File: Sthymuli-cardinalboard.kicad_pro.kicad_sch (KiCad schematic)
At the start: 38 parts, among them J8 Conn_02x08_Counter_Clockwise, Q10 NX7002AK, Q11 NX7002AK, Q12 NX7002AK, Q13 NX7002AK, SW10 SW_Push, SW7 SW_Push, SW8 SW_Push, SW9 SW_Push, U13 LSM6DS3, U17 ITR9909, U18 ITR9909, U19 ITR9909, U20 ITR9909

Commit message: routing small board
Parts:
- removed Q12, Q13: NX7002AK, Package_TO_SOT_SMD:SOT-23, symbol Transistor_FET_Other:Q_NMOS_Depletion_GSD
- removed R54, R55: 3K3, Capacitor_SMD:C_0201_0603Metric, symbol Device:R
- removed R64, R65: 27R, Capacitor_SMD:C_0201_0603Metric, symbol Device:R
- removed SW10, SW9: SW_Push, sthymuli:XKB5858, symbol Switch:SW_Push
- removed U19, U20: ITR9909, sthymuli:ITR_9909_Vertical, symbol kitprisme:ITR9909
- J1: renamed from J8; footprint (none) -> Connector_PinSocket_2.54mm:PinSocket_2x08_P2.54mm_Vertical_SMD
- U2: renamed from U18; footprint sthymuli:ITR_9909_Horizontal -> sthymuli:ITR_9909_Vertical
- renumbered C20 to C1, C21 to C2, C22 to C3, C23 to C4, C24 to C5, C25 to C6, C77 to C7, D20 to D1, D26 to D2, D21 to D3, D22 to D4, D23 to D5, D24 to D6, D25 to D7, Q10 to Q1, Q11 to Q2, R52 to R1, R53 to R2, R62 to R3, R63 to R4, SW7 to SW1, SW8 to SW2, U17 to U1, U13 to U3
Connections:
- net ACC_B_INT1 is gone; now on net +3V3: J1.2 (Pin_2)
- net btn_EAST_DOWN is gone; now on net btn_DOWN: J1.4 (Pin_4)
- net btn_EAST_UP is gone; now on net IR_TRA_VERT: J1.13 (Pin_13)
- net +3V3: no longer J1.1 (Pin_1)
- net +5V: now also J1.1 (Pin_1); no longer J1.16 (Pin_16)
- net BAT+: now also J1.6 (Pin_6); no longer J1.7 (Pin_7)
- net BAT-: now also J1.7 (Pin_7); no longer J1.10 (Pin_10)
- net DIN: now also J1.8 (Pin_8); no longer J1.3 (Pin_3)
- net DOUT: now also J1.9 (Pin_9); no longer J1.14 (Pin_14)
- net GND: now also J1.3 (Pin_3); no longer J1.15 (Pin_15)
- net SCL: now also J1.15 (Pin_15); no longer J1.9 (Pin_9)
- net SDA: now also J1.14 (Pin_14); no longer J1.8 (Pin_8)
- net btn_UP: now also J1.5 (Pin_5)
- net ACC_INT: now reaches U3.4 (INT1)
- net ACC_INT: now also J1.16 (Pin_16)
- net IR_REC_2 renamed IR_REC_HORI
- net IR_REC_HORI: now also J1.10 (Pin_10); no longer J1.5 (Pin_5)
- net IR_REC_3 renamed IR_REC_VERT
- net IR_REC_VERT: now also J1.12 (Pin_12); no longer J1.6 (Pin_6)
- net IR_TRA_2 renamed IR_TRA_HORI
- net IR_TRA_HORI: now also J1.11 (Pin_11); no longer J1.12 (Pin_12)
- net IR_TRA_3 renamed IR_TRA_VERT
- net IR_TRA_VERT: no longer J1.11 (Pin_11)
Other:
- note removed: "Buttons/switch"
- note removed: "we use MCP23017 internal pull-ups"
- moved on the sheet: BT1, C1, C2, C3, C4, C5, C6, C7, D1, D2, D3, D4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

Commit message: tried autoroute...
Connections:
- net btn_DOWN renamed btn_A
- net btn_UP renamed btn_B
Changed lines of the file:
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@@
 		)
 	)
-	(global_label "btn_DOWN"
+	(global_label "btn_A"
 		(shape input)
 		(at 48.26 142.24 90)
@@
 		)
 		(property "Intersheetrefs" "${INTERSHEET_REFS}"
-			(at 48.26 129.8811 90)
+			(at 48.26 134.1749 90)
 			(hide yes)
 			(show_name no)
@@
 		)
 	)
-	(global_label "btn_UP"
+	(global_label "btn_B"
 		(shape input)
 		(at 53.34 140.97 90)
@@
 		)
 		(property "Intersheetrefs" "${INTERSHEET_REFS}"
-			(at 53.34 131.393 90)
+			(at 53.34 132.7235 90)
 			(hide yes)
 			(show_name no)
@@
 		)
 	)
-	(global_label "btn_DOWN"
+	(global_label "btn_A"
 		(shape input)
 		(at 130.81 66.04 180)
@@
 		)
 		(property "Intersheetrefs" "${INTERSHEET_REFS}"
-			(at 118.4511 66.04 0)
+			(at 122.7449 66.04 0)
 			(hide yes)
 			(show_name no)
@@
 		)
 	)
-	(global_label "btn_UP"
+	(global_label "btn_B"
 		(shape input)
 		(at 130.81 68.58 180)
@@
 		)
 		(property "Intersheetrefs" "${INTERSHEET_REFS}"
-			(at 121.233 68.58 0)
-			(hide yes)
-			(show_name no)
+			(at 122.5635 68.58 0)
+			(hide yes)
+			(show_name no)

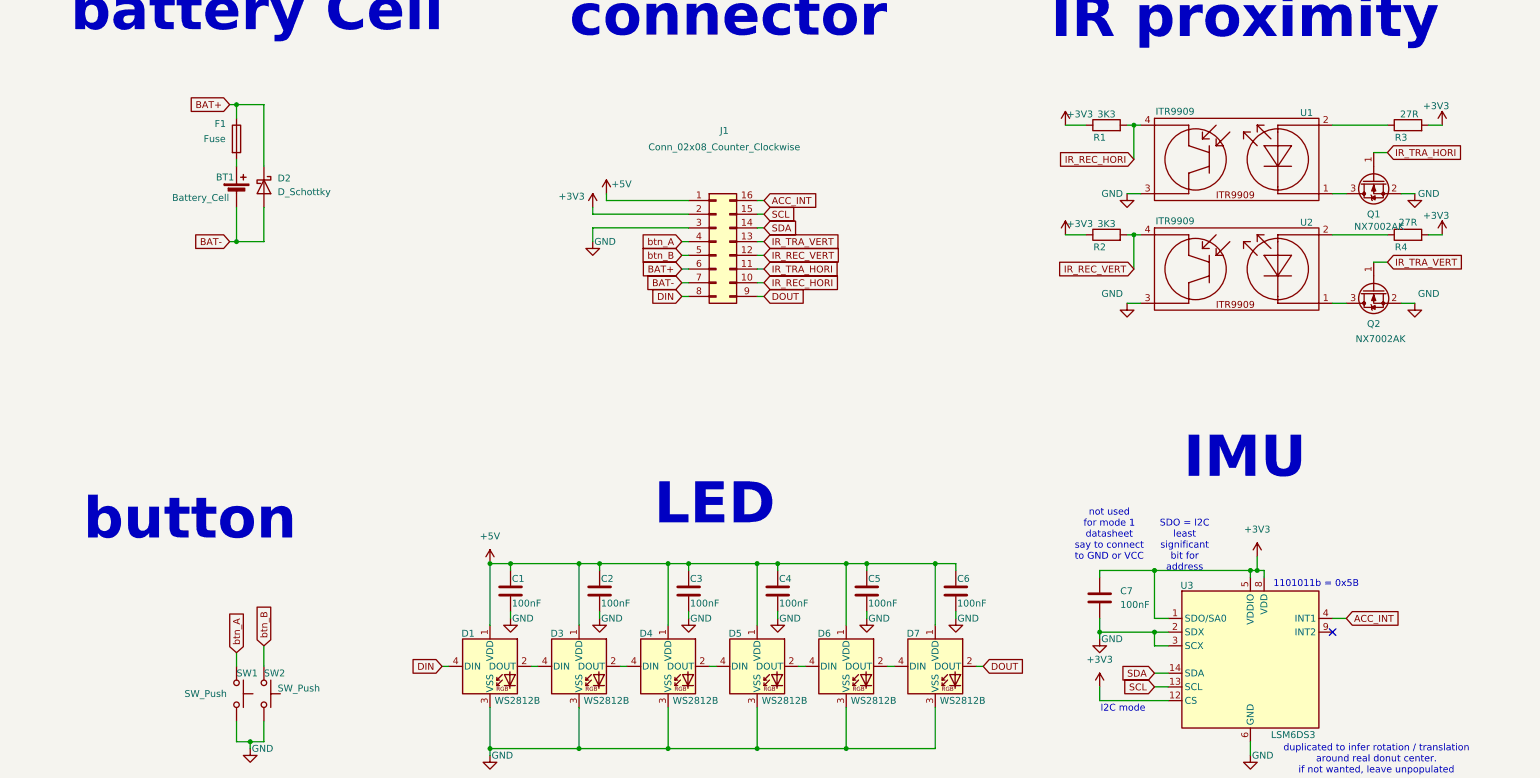
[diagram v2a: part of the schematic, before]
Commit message: fixed resistor footprint, enabled all DRC, improved readability
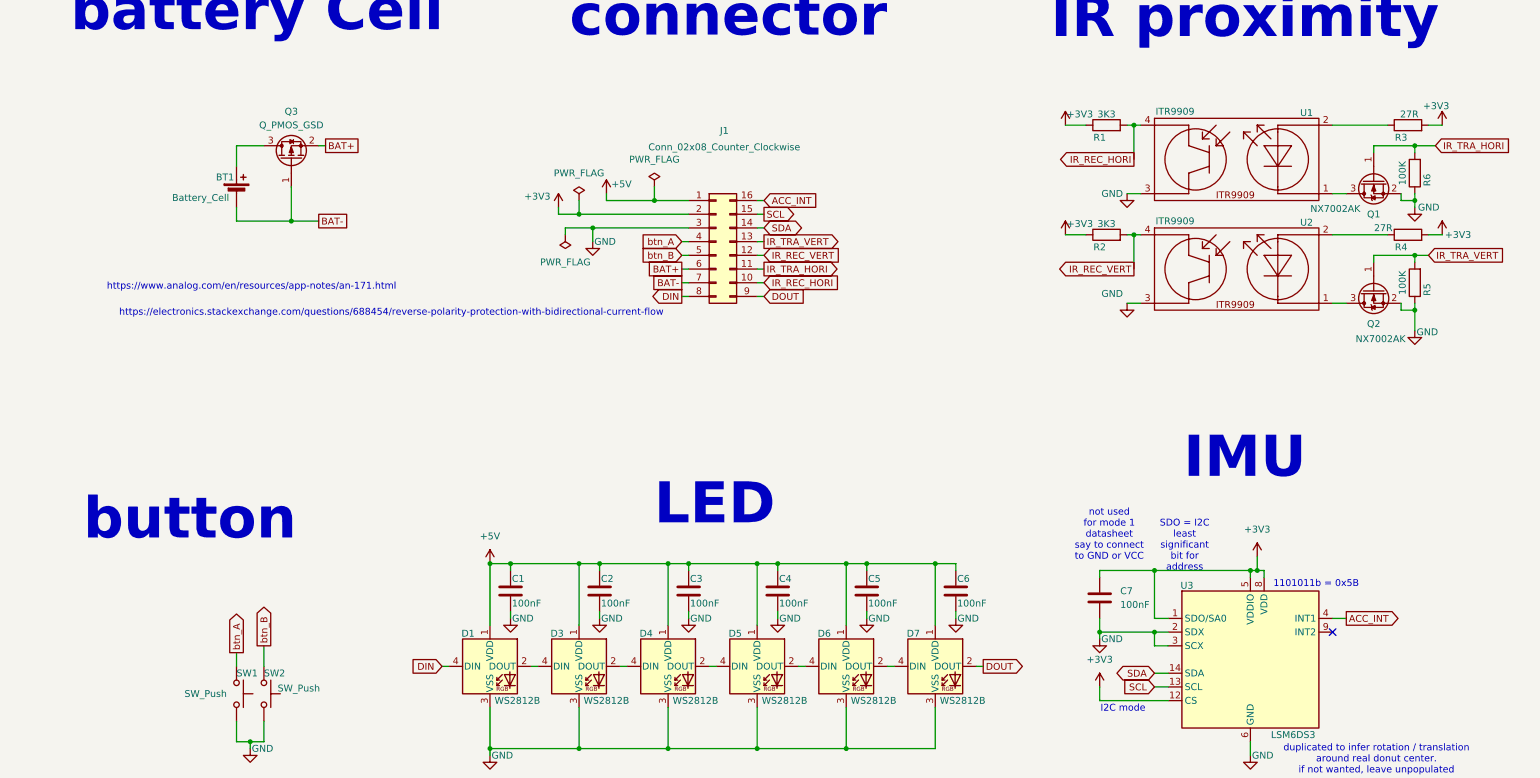
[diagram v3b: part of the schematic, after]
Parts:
- removed D2: D_Schottky, Diode_SMD:D_SOD-123F, symbol Device:D_Schottky
- removed F1: Fuse, Resistor_SMD:R_0805_2012Metric, symbol Device:Fuse
- added Q3: Q_PMOS_GSD, Package_TO_SOT_SMD:TSOT-23, symbol Transistor_FET:Q_PMOS_GSD
- added R5, R6: 100K, Resistor_SMD:R_0603_1608Metric, symbol Device:R
- R1, R2, R3, R4: footprint Capacitor_SMD:C_0201_0603Metric -> Resistor_SMD:R_0603_1608Metric
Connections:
- net BAT+: now also Q3.2 (S)
- net BAT-: now also Q3.1 (G)
- net GND: now also R5.1, R6.1
- net IR_TRA_HORI: now also R6.2
- net IR_TRA_VERT: now also R5.2
- net at BT1.1 (+): now also Q3.3 (D)
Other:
- note added: "https://electronics.stackexchange.com/questions/688454/reverse-polarity-protection-with-bidirectional-current-flow"
- note added: "https://www.analog.com/en/resources/app-notes/an-171.html"
